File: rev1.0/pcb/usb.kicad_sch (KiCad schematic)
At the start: 12 parts, among them J2 USB4120-03-C, U2 USBLC6-2SC6

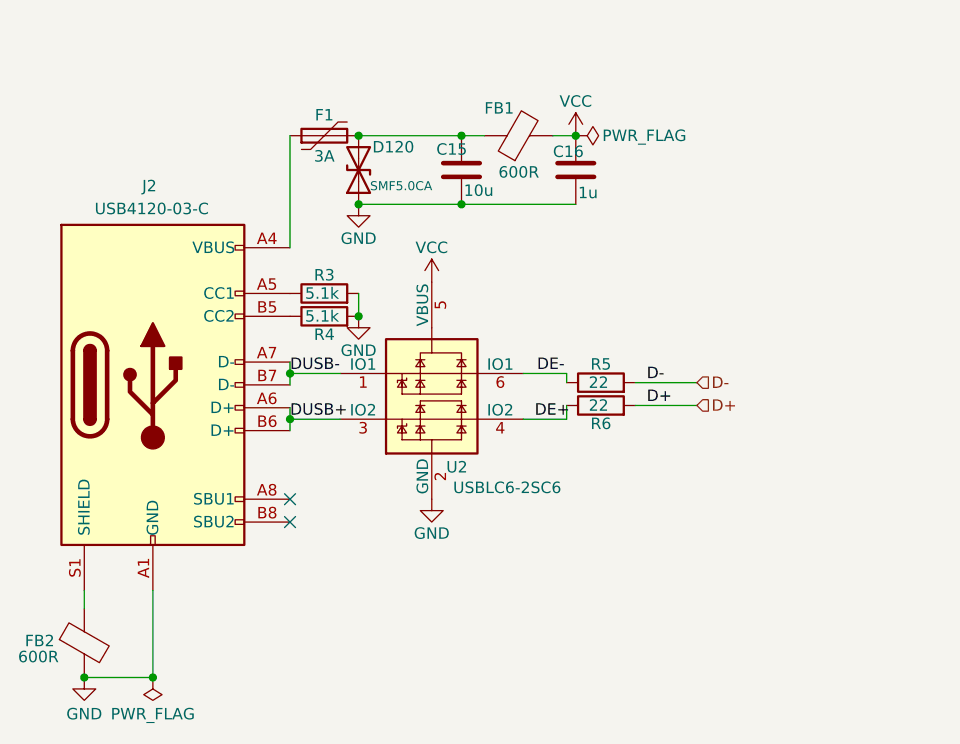
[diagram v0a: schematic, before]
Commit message: rp2040 port: updated schematic and fixed footprints
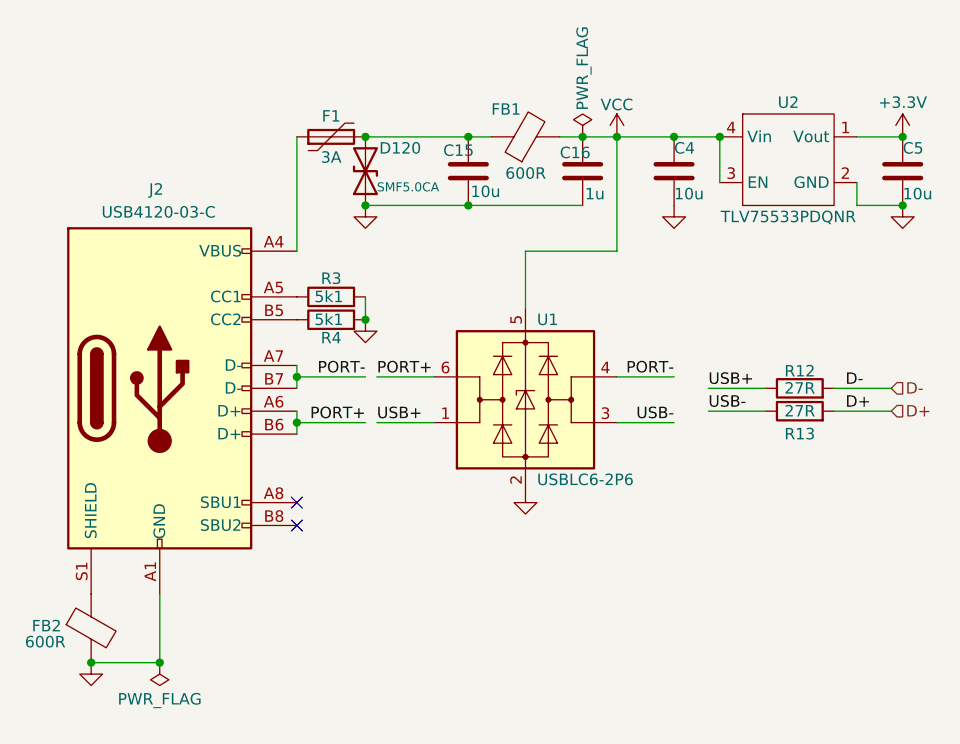
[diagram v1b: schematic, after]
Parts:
- removed R5, R6: 22, Resistor_SMD:R_0603_1608Metric, symbol Device:R
- removed U2: USBLC6-2SC6, Package_TO_SOT_SMD:SOT-23-6, symbol 0xcb:USBLC6-2SC6
- added C4, C5: 10u, Capacitor_SMD:C_0201_0603Metric, symbol Device:C
- added R12, R13: 27R, Resistor_SMD:R_0201_0603Metric, symbol Device:R
- added U1: USBLC6-2P6, Package_TO_SOT_SMD:SOT-666, symbol Power_Protection:USBLC6-2P6
- added U2: TLV75533PDQNR, 0xcb:X2SON-4, symbol 0xcb:LP5907SNX-3.3-NOPB
- C15, C16: footprint Capacitor_SMD:C_0603_1608Metric -> Capacitor_SMD:C_0201_0603Metric
- FB1, FB2: footprint 0xcb:Ferrite_Bead_0603 -> Capacitor_SMD:C_0201_0603Metric
- R3, R4: value 5.1k -> 5k1; footprint Resistor_SMD:R_0603_1608Metric -> Resistor_SMD:R_0201_0603Metric
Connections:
- net D+: now also R13.2
- net D-: now also R12.2
- net GND: now also C4.2, C5.2, U1.2 (GND), U2.2 (GND), U2.5 (TP)
- net VCC: now also C4.1, U1.5 (VBUS), U2.3 (EN), U2.4 (Vin)
- net DUSB+ renamed PORT+
- net PORT+: now also U1.6 (I/O1)
- net DUSB- renamed PORT-
- net PORT-: now also U1.4 (I/O2)
- new net +3.3V: C5.1, U2.1 (Vout)
- new net USB+: R12.1, U1.1 (I/O1)
- new net USB-: R13.1, U1.3 (I/O2)
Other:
- moved on the sheet: C15, C16, D120, F1, FB1, FB2, J2, R3, R4

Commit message: fixup and add prod
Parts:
- C15: footprint Capacitor_SMD:C_0201_0603Metric -> Capacitor_SMD:C_0402_1005Metric; LCSC (none) -> C15525
- C16: LCSC (none) -> C237458
- C4, C5: footprint Capacitor_SMD:C_0201_0603Metric -> Capacitor_SMD:C_0402_1005Metric
- D120: JLCPCB_CORRECTION (none) -> 0; 0; 180; LCSC (none) -> C399251
- F1: LCSC (none) -> C70156
- FB1, FB2: LCSC (none) -> C88960
- J2: JLCPCB_CORRECTION (none) -> 0; 2.5; 180; LCSC (none) -> C165948
- R12, R13: JLCPCB_CORRECTION (none) -> 0; 0; 90; LCSC C25100 -> C273295
- R3, R4: LCSC (none) -> C473460
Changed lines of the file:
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@@
       (effects (font (size 1.27 1.27)) hide)
     )
-    (property "LCSC" "C25100" (at 149.86 63.5 0)
+    (property "LCSC" "C273295" (at 149.86 63.5 0)
       (effects (font (size 1.27 1.27)) hide)
     )
@@
     )
     (property "Substitute" "Y" (at 149.86 63.5 0)
+      (effects (font (size 1.27 1.27)) hide)
+    )
+    (property "JLCPCB_CORRECTION" "0; 0; 90" (at 149.86 63.5 0)
       (effects (font (size 1.27 1.27)) hide)
     )
@@
       (effects (font (size 1.27 1.27)) (justify left))
     )
-    (property "Footprint" "Capacitor_SMD:C_0201_0603Metric" (at 136.8552 43.18 0)
+    (property "Footprint" "Capacitor_SMD:C_0402_1005Metric" (at 136.8552 43.18 0)
       (effects (font (size 1.27 1.27)) hide)
     )
@@
       (effects (font (size 1.27 1.27)) hide)
     )
+    (property "LCSC" "C237458" (at 125.73 39.37 0)
+      (effects (font (size 1.27 1.27)) hide)
+    )
     (pin "1")
     (pin "2")
@@
     )
     (property "Datasheet" "~" (at 97.79 53.34 0)
+      (effects (font (size 1.27 1.27)) hide)
+    )
+    (property "LCSC" "C473460" (at 97.79 53.34 0)
+      (effects (font (size 1.27 1.27)) hide)
+    )
+    (property "JLCPCB_CORRECTION" "" (at 97.79 53.34 0)
       (effects (font (size 1.27 1.27)) hide)
     )
@@
       (effects (font (size 1.27 1.27)) hide)
     )
+    (property "LCSC" "C70156" (at 97.79 35.56 0)
+      (effects (font (size 1.27 1.27)) hide)
+    )
     (pin "1")
     (pin "2")
@@
       (effects (font (size 1.27 1.27)) hide)
     )
+    (property "LCSC" "C473460" (at 97.79 55.88 0)
+      (effects (font (size 1.27 1.27)) hide)
+    )
+    (property "JLCPCB_CORRECTION" "" (at 97.79 55.88 0)
+      (effects (font (size 1.27 1.27)) hide)
+    )
     (pin "1")
     (pin "2")
@@
     )
     (property "Datasheet" "https://www.usb.org/sites/default/files/documents/usb_type-c.zip" (at 82.55 63.5 0)
+      (effects (font (size 1.27 1.27)) hide)
+    )
+    (property "LCSC" "C165948" (at 78.74 63.5 0)
+      (effects (font (size 1.27 1.27)) hide)
+    )
+    (property "JLCPCB_CORRECTION" "0; 2.5; 180" (at 78.74 63.5 0)
       (effects (font (size 1.27 1.27)) hide)
     )
@@
       (effects (font (size 1.27 1.27)) hide)
     )
+    (property "LCSC" "C88960" (at 119.38 35.56 0)
+      (effects (font (size 1.27 1.27)) hide)
+    )
     (pin "1")
     (pin "2")
@@
       (effects (font (size 1.27 1.27)) hide)
     )
-    (property "LCSC" "C25100" (at 149.86 66.04 0)
+    (property "LCSC" "C273295" (at 149.86 66.04 0)
       (effects (font (size 1.27 1.27)) hide)
     )
@@
     )
     (property "Substitute" "Y" (at 149.86 66.04 0)
+      (effects (font (size 1.27 1.27)) hide)
+    )
+    (property "JLCPCB_CORRECTION" "0; 0; 90" (at 149.86 66.04 0)
       (effects (font (size 1.27 1.27)) hide)
     )
@@
       (effects (font (size 1.27 1.27)) hide)
     )
+    (property "LCSC" "C88960" (at 71.12 90.17 0)
+      (effects (font (size 1.27 1.27)) hide)
+    )
     (pin "1")
     (pin "2")
@@
     )
     (property "Datasheet" "~" (at 101.6 39.37 0)
+      (effects (font (size 1.27 1.27)) hide)
+    )
+    (property "LCSC" "C399251" (at 101.6 39.37 0)
+      (effects (font (size 1.27 1.27)) hide)
+    )
+    (property "JLCPCB_CORRECTION" "0; 0; 180" (at 101.6 39.37 0)
       (effects (font (size 1.27 1.27)) hide)
     )
@@
       (effects (font (size 1.27 1.27)) (justify left))
     )
-    (property "Footprint" "Capacitor_SMD:C_0201_0603Metric" (at 162.2552 43.18 0)
+    (property "Footprint" "Capacitor_SMD:C_0402_1005Metric" (at 162.2552 43.18 0)
       (effects (font (size 1.27 1.27)) hide)
     )
@@
       (effects (font (size 1.27 1.27)) (justify left))
     )
-    (property "Footprint" "Capacitor_SMD:C_0201_0603Metric" (at 113.9952 43.18 0)
+    (property "Footprint" "Capacitor_SMD:C_0402_1005Metric" (at 113.9952 43.18 0)
       (effects (font (size 1.27 1.27)) hide)
     )
@@
       (effects (font (size 1.27 1.27)) hide)
     )
+    (property "LCSC" "C15525" (at 113.03 39.37 0)
+      (effects (font (size 1.27 1.27)) hide)
+    )
